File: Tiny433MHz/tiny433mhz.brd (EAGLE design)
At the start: 23.2 x 17.5 mm, 10 parts, among them U1 ATTINY85V-10SU

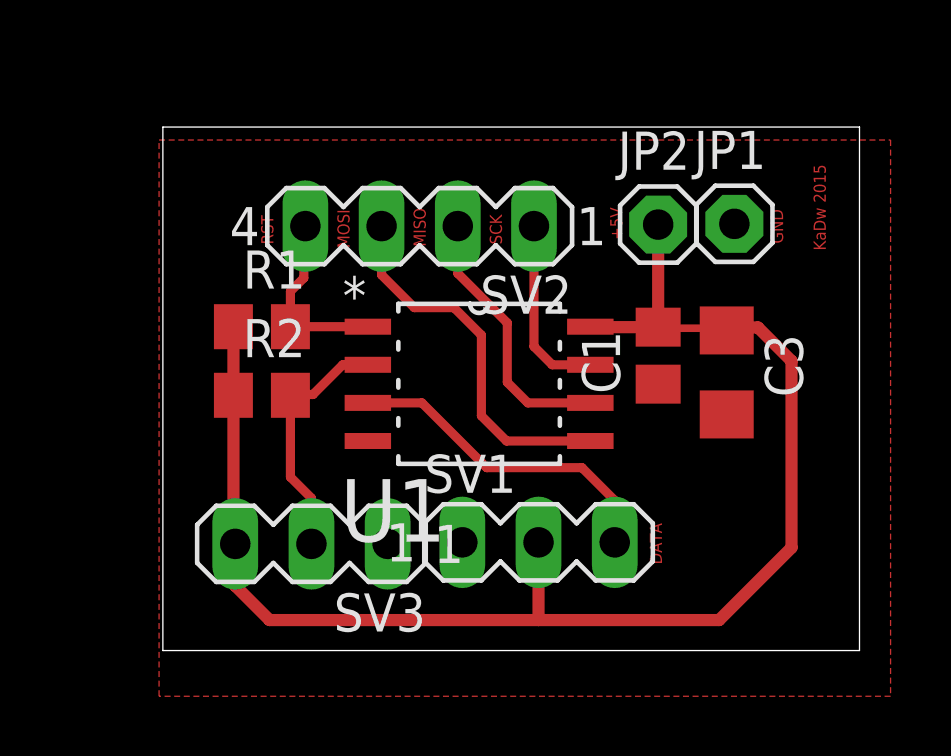
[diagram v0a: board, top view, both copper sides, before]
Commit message: updated WiSwitch, tiny433mhz and ade7953
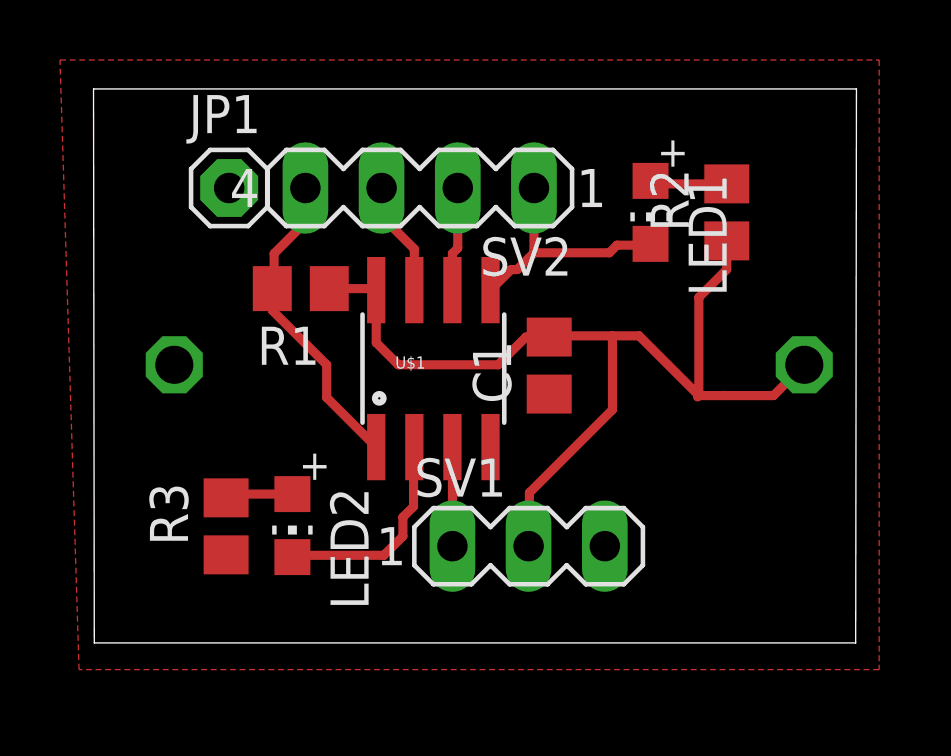
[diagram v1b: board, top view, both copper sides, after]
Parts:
- removed C3: 10uF, rcl:C1206
- removed JP2: (no value), adafruit:1X01
- removed SV3: (no value), con-lstb:MA03-1
- removed U1: ATTINY85V-10SU, atmel:SOIC127P798X216-8N
- added LED1, LED2: (no value), adafruit:CHIP-LED0805
- added R3: 10k, rcl:R0805
- added U$1: ATTINY13SOIC, SparkFun:SO08
- added U$3: CR2032, _CR2032:CR2032-THT
- R2: value 4,7k -> 10k
- moved JP1 16.9 mm to (0.56, 99.2)
- moved R2 16.7 mm to (17.1, 98.4), turned to 90 degrees
- moved C1 3.65 mm to (11.2, 93.3)
- moved R1 1.81 mm to (2.95, 95.9), turned to 180 degrees
- moved SV2 1.27 mm to (6.91, 99.2)
- moved SV1 0.35 mm to (10.5, 87.3)
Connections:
- removed net 1WIRE: R2.2, SV3.2, U1.2
- new net LED: LED2.C, U$1.2
- new net N$1: LED2.A, R3.2
- new net N$2: LED1.A, R2.2
- net DATA: now also SV1.1, U$1.3; no longer SV1.3, U1.3
- net GND: now also R3.1, SV1.3, U$1.4, U$3.-; no longer C3.2, SV1.1, SV3.1, U1.4
- net MISO: now also U$1.6; no longer U1.6
- net MOSI: now also LED1.C, SV2.1, U$1.5; no longer SV2.3, U1.5
- net RESET: now also U$1.1; no longer U1.1
- net SCK: now also SV2.3, U$1.7; no longer SV2.1, U1.7
- net VCC: now also U$1.8, U$3.+; no longer C3.1, JP2.1, SV3.3, U1.8
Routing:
- net VCC: track 50.6 -> 33.4 mm
- net 1WIRE: track 8.24 -> 0.00 mm
- net DATA: track 11.0 -> 3.34 mm
- net LED: track 0.00 -> 7.15 mm
- net MISO: track 8.94 -> 3.48 mm
- net RESET: track 6.14 -> 10.5 mm
- net MOSI: track 12.5 -> 8.13 mm
- net N$2: track 0.00 -> 2.58 mm
- net SCK: track 6.15 -> 3.86 mm
- net N$1: track 0.00 -> 2.26 mm
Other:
- board size 23.2 x 17.5 mm -> 25.4 x 18.5 mm
- board text removed: "+5V"
- board text removed: "DATA"
- board text removed: "GND"
- board text removed: "KaDw 2015"
- board text removed: "MISO"
- board text removed: "MOSI"
- board text removed: "RST"
- board text removed: "SCK"
